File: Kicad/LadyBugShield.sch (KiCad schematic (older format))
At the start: 1 part

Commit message: update
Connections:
- wire segments 78 -> 75
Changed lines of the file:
@@
 Sheet 1 8
 Title ""
-Date "4 dec 2014"
+Date "8 dec 2014"
 Rev ""
 Comp ""
@@
 F9 "ALERT" I R 3300 2600 60
 F10 "Vin" O L 800 5250 60
-F11 "Measure_pH_or_Temp" O R 3300 2950 60
+F11 "Therm_AIN" I R 3300 4200 60
 $EndSheet
 $Sheet
@@
 F7 "pH_AIN" I R 5950 2050 60
 F8 "EC_AIN" I R 5950 2300 60
-F9 "Therm_AIN" I R 5950 2550 60
-F10 "VGND" I R 5950 2800 60
-F11 "Measure_pH_or_Temp" I L 4050 2950 60
+F9 "VGND" I R 5950 2800 60
 $EndSheet
 $Sheet
@@
 	6600 2300 5950 2300
 Wire Wire Line
-	6750 4200 6450 4200
-Wire Wire Line
-	6450 4200 6450 2550
-Wire Wire Line
-	6450 2550 5950 2550
-Wire Wire Line
 	5950 2800 6350 2800
 Wire Wire Line
@@
 Connection ~ 6350 6850
 Wire Wire Line
-	3300 2950 4050 2950
+	3300 4200 6750 4200
 $EndSCHEMATC

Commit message: first pass at layout
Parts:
- removed P?: CONN_12, symbol CONN_12
- added P1: CONN_6, symbol CONN_6
- added P2: CONN_2, symbol CONN_2
- added P3, P4: BNC, ~, symbol BNC
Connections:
- net labels added: VGND, Vclean
- wire segments 75 -> 25

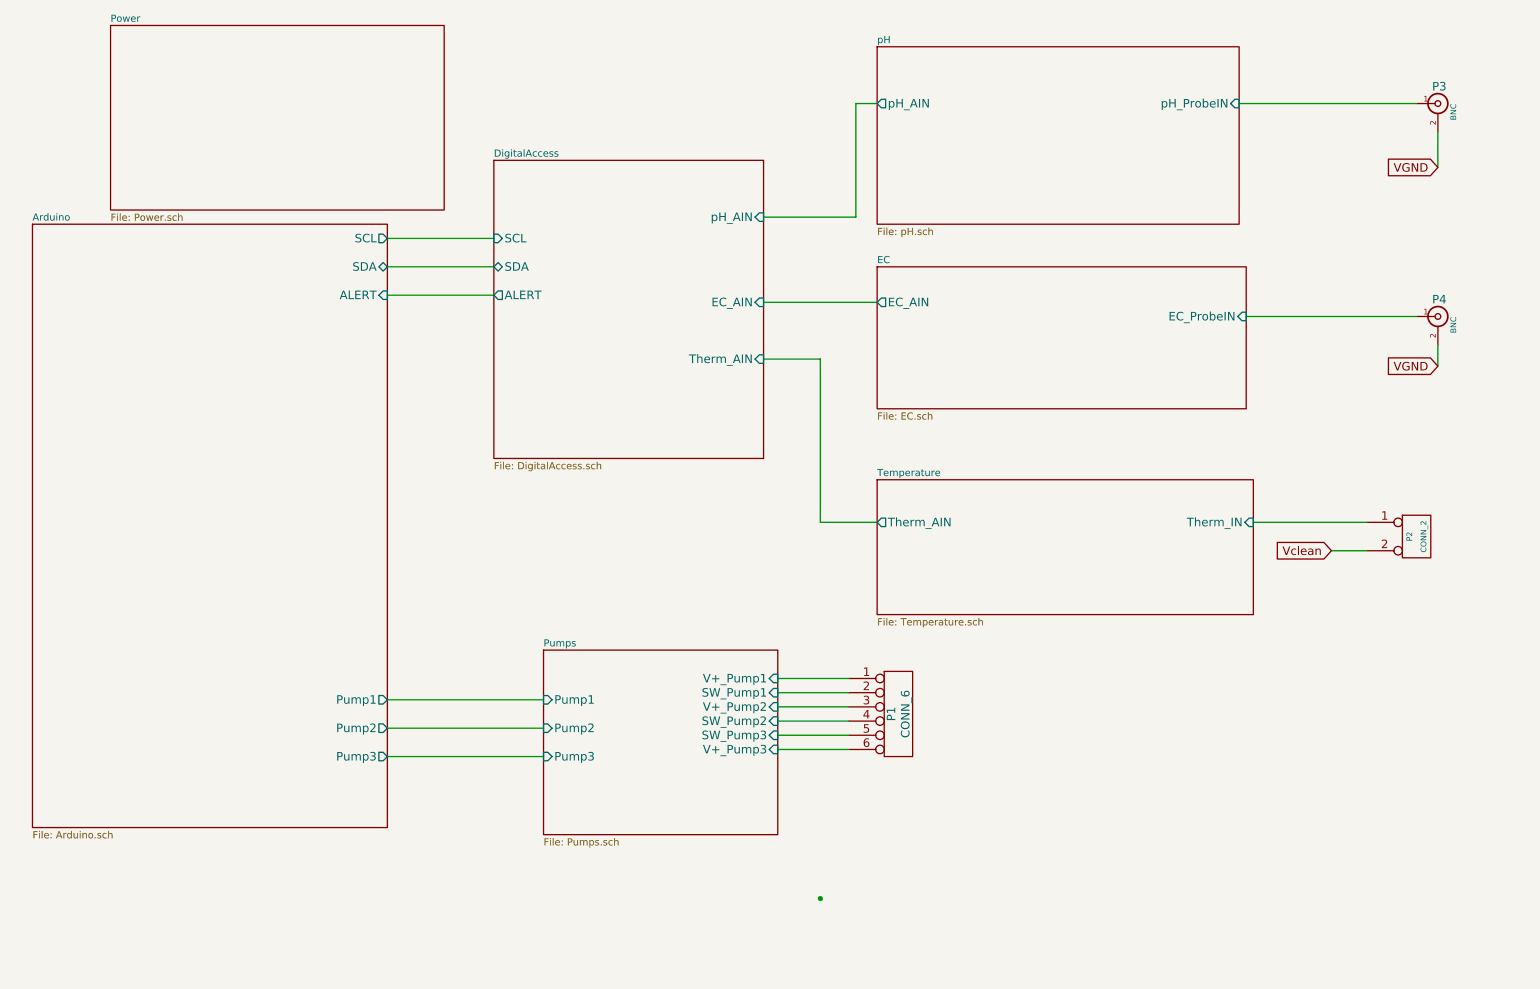
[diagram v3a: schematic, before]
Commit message: changed diodes added test points
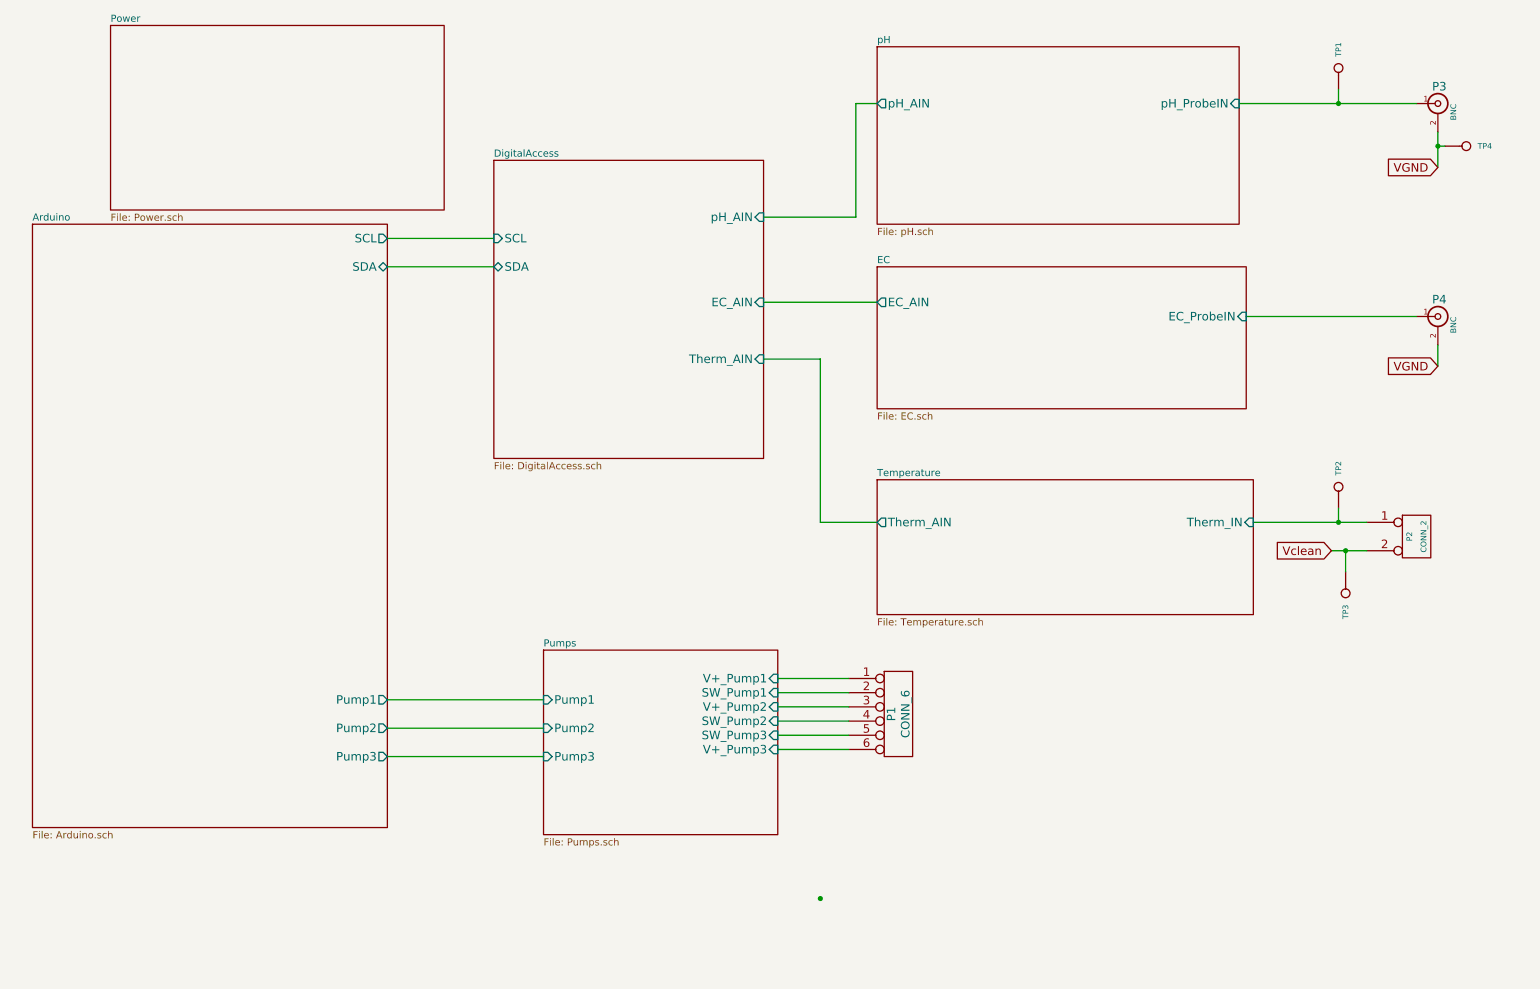
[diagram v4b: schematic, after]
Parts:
- added TP1, TP2, TP3, TP4: CONN_1, symbol CONN_1
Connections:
- net Temperature/Therm_IN: now also TP2.1
- net VGND: now also TP4.1
- net Vclean: now also TP3.1
- net pH/pH_ProbeIN: now also TP1.1
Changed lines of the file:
@@
 Sheet 1 8
 Title ""
-Date "18 dec 2014"
+Date "20 dec 2014"
 Rev ""
 Comp ""
@@
 F5 "Pump1" O R 3300 5450 60
 F6 "Pump3" O R 3300 5850 60
-F7 "ALERT" I R 3300 2600 60
 $EndSheet
 $Sheet
@@
 F2 "SCL" I L 4050 2200 60
 F3 "SDA" B L 4050 2400 60
-F4 "ALERT" O L 4050 2600 60
-F5 "pH_AIN" I R 5950 2050 60
-F6 "EC_AIN" I R 5950 2650 60
-F7 "Therm_AIN" I R 5950 3050 60
+F4 "pH_AIN" I R 5950 2050 60
+F5 "EC_AIN" I R 5950 2650 60
+F6 "Therm_AIN" I R 5950 3050 60
 $EndSheet
 $Sheet
@@
 Wire Wire Line
 	3300 2400 4050 2400
-Wire Wire Line
-	3300 2600 4050 2600
 Connection ~ 6350 6850
 $Sheet
@@
 Wire Wire Line
 	6050 5800 6550 5800
+$Comp
+L CONN_1 TP1
+U 1 1 54956214
+P 10000 1000
+F 0 "TP1" H 10080 1000 40  0000 L CNN
+F 1 "CONN_1" H 10000 1055 30  0001 C CNN
+F 2 "" H 10000 1000 60  0000 C CNN
+F 3 "" H 10000 1000 60  0000 C CNN
+	1    10000 1000
+	0    -1   -1   0
+$EndComp
+$Comp
+L CONN_1 TP4
+U 1 1 54956279
+P 10900 1550
+F 0 "TP4" H 10980 1550 40  0000 L CNN
+F 1 "CONN_1" H 10900 1605 30  0001 C CNN
+F 2 "" H 10900 1550 60  0000 C CNN
+F 3 "" H 10900 1550 60  0000 C CNN
+	1    10900 1550
+	1    0    0    -1
+$EndComp
+$Comp
+L CONN_1 TP2
+U 1 1 5495627F
+P 10000 3950
+F 0 "TP2" H 10080 3950 40  0000 L CNN
+F 1 "CONN_1" H 10000 4005 30  0001 C CNN
+F 2 "" H 10000 3950 60  0000 C CNN
+F 3 "" H 10000 3950 60  0000 C CNN
+	1    10000 3950
+	0    -1   -1   0
+$EndComp
+$Comp
+L CONN_1 TP3
+U 1 1 54956285
+P 10050 4700
+F 0 "TP3" H 10130 4700 40  0000 L CNN
+F 1 "CONN_1" H 10050 4755 30  0001 C CNN
+F 2 "" H 10050 4700 60  0000 C CNN
+F 3 "" H 10050 4700 60  0000 C CNN
+	1    10050 4700
+	0    1    1    0
+$EndComp
+Wire Wire Line
+	10000 1150 10000 1250
+Connection ~ 10000 1250
+Wire Wire Line
+	10750 1550 10700 1550
+Connection ~ 10700 1550
+Wire Wire Line
+	10000 4100 10000 4200
+Connection ~ 10000 4200
+Wire Wire Line
+	10050 4550 10050 4400
+Connection ~ 10050 4400
 $EndSCHEMATC

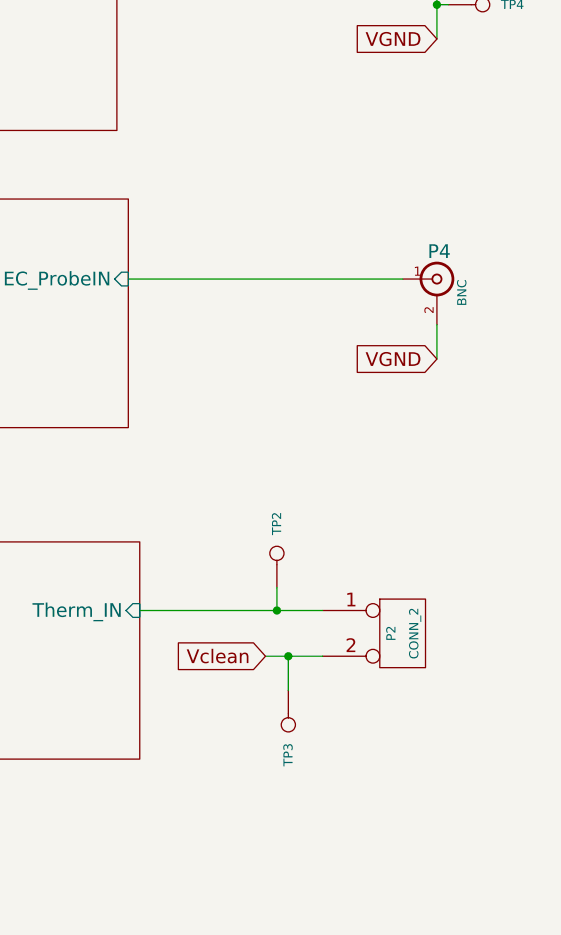
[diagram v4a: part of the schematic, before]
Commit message: moved component reference and value for placing components
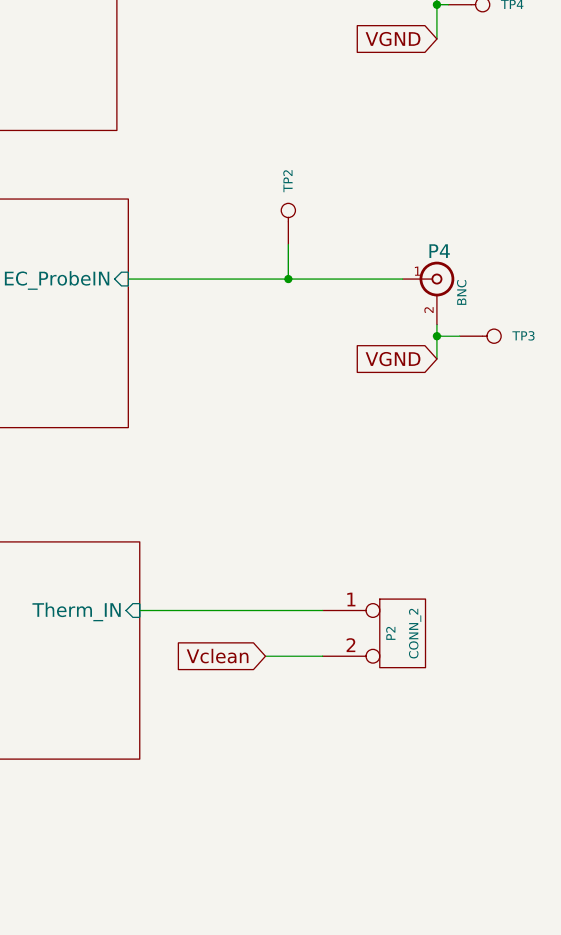
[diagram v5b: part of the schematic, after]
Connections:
- net EC/EC_ProbeIN: now also TP2.1
- net Temperature/Therm_IN: no longer TP2.1
- net VGND: now also TP3.1
- net Vclean: no longer TP3.1
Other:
- moved on the sheet: TP2, TP3
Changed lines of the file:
@@
 L CONN_1 TP2
 U 1 1 5495627F
-P 10000 3950
-F 0 "TP2" H 10080 3950 40  0000 L CNN
-F 1 "CONN_1" H 10000 4005 30  0001 C CNN
-F 2 "" H 10000 3950 60  0000 C CNN
-F 3 "" H 10000 3950 60  0000 C CNN
-	1    10000 3950
+P 10050 2450
+F 0 "TP2" H 10130 2450 40  0000 L CNN
+F 1 "CONN_1" H 10050 2505 30  0001 C CNN
+F 2 "" H 10050 2450 60  0000 C CNN
+F 3 "" H 10050 2450 60  0000 C CNN
+	1    10050 2450
 	0    -1   -1   0
 $EndComp
@@
 L CONN_1 TP3
 U 1 1 54956285
-P 10050 4700
-F 0 "TP3" H 10130 4700 40  0000 L CNN
-F 1 "CONN_1" H 10050 4755 30  0001 C CNN
-F 2 "" H 10050 4700 60  0000 C CNN
-F 3 "" H 10050 4700 60  0000 C CNN
-	1    10050 4700
-	0    1    1    0
+P 10950 3000
+F 0 "TP3" H 11030 3000 40  0000 L CNN
+F 1 "CONN_1" H 10950 3055 30  0001 C CNN
+F 2 "" H 10950 3000 60  0000 C CNN
+F 3 "" H 10950 3000 60  0000 C CNN
+	1    10950 3000
+	1    0    0    -1
 $EndComp
 Wire Wire Line
@@
 Connection ~ 10700 1550
 Wire Wire Line
-	10000 4100 10000 4200
-Connection ~ 10000 4200
+	10050 2600 10050 2750
+Connection ~ 10050 2750
 Wire Wire Line
-	10050 4550 10050 4400
-Connection ~ 10050 4400
+	10800 3000 10700 3000
+Connection ~ 10700 3000
 $EndSCHEMATC

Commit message: updates based on reviewing layout
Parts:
- removed TP3, TP4: CONN_1, symbol CONN_1
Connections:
- net Pumps/SW_Pump3: now also P1.6; no longer P1.5
- net Pumps/V+_Pump3: now also P1.5; no longer P1.6
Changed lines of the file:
@@
 Sheet 1 8
 Title ""
-Date "23 dec 2014"
+Date "27 dec 2014"
 Rev ""
 Comp ""
@@
 F7 "V+_Pump2" I R 6050 5500 60
 F8 "Pump3" I L 4400 5850 60
-F9 "SW_Pump3" I R 6050 5700 60
-F10 "V+_Pump3" I R 6050 5800 60
+F9 "SW_Pump3" I R 6050 5800 60
+F10 "V+_Pump3" I R 6050 5700 60
 $EndSheet
 Wire Wire Line
@@
 $EndComp
 $Comp
-L CONN_1 TP4
-U 1 1 54956279
-P 10900 1550
-F 0 "TP4" H 10980 1550 40  0000 L CNN
-F 1 "CONN_1" H 10900 1605 30  0001 C CNN
-F 2 "" H 10900 1550 60  0000 C CNN
-F 3 "" H 10900 1550 60  0000 C CNN
-	1    10900 1550
-	1    0    0    -1
-$EndComp
-$Comp
 L CONN_1 TP2
 U 1 1 5495627F
@@
 	0    -1   -1   0
 $EndComp
-$Comp
-L CONN_1 TP3
-U 1 1 54956285
-P 10950 3000
-F 0 "TP3" H 11030 3000 40  0000 L CNN
-F 1 "CONN_1" H 10950 3055 30  0001 C CNN
-F 2 "" H 10950 3000 60  0000 C CNN
-F 3 "" H 10950 3000 60  0000 C CNN
-	1    10950 3000
-	1    0    0    -1
-$EndComp
 Wire Wire Line
 	10000 1150 10000 1250
 Connection ~ 10000 1250
 Wire Wire Line
-	10750 1550 10700 1550
-Connection ~ 10700 1550
-Wire Wire Line
 	10050 2600 10050 2750
 Connection ~ 10050 2750
-Wire Wire Line
-	10800 3000 10700 3000
-Connection ~ 10700 3000
 $EndSCHEMATC
